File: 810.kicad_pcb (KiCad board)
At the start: 2 copper layers, 148 x 110 mm, 308 parts, among them J1 PJ301BM, J10 PJ301BM, J11 PJ301BM, J12 PJ301BM, J13 PJ301BM, J14 PJ301BM, J15 JACK_MONO_SW, J16 PJ301BM, J17 PJ301B, J18 PJ301B, J2 PJ301BM, J3 PJ301BM, J4 PJ301B, J5 PJ301B, J6 PJ301BM, J7 PJ301BM, J8 PJ301BM, J9 PJ301BM, P1 CONN_01X08, P2 CONN_02X05, P3 CONN_01X03, P4 CONN_01X08, Q1 PMBT2369, Q10 2SK208-GR, Q11 2SC4738, Q12 2SA1832, Q13 2SA1832, Q14 2SA1832, Q15 2SC4738, Q2 2SK208-GR, Q3 2SA1618, Q4 2SC4207, Q5 2SK208-GR, Q6 MMBF4391LT1G, Q7 2SA1832, Q8 PMBT2369, Q9 2SK208-GR, SW1 SPDT, SW2 SPDT, SW3 BF3-1050, SW4 SPDT, SW5 DP6T-ALPHA-SR2511, U1 TL072-, U10 TL072-, U11 TL072-, U12 TA75S558F, U13 TA75S558F, U14 TA75S558F, U15 TA75S558F, U16 TA75S558F, U17 CD4052, U18 TA75S558F, U2 TL072-, U3 TL072-, U4 CD40106, U5 CD4027, U6 LM13700, U7 LM13700, U8 LM13700, U9 TL072-

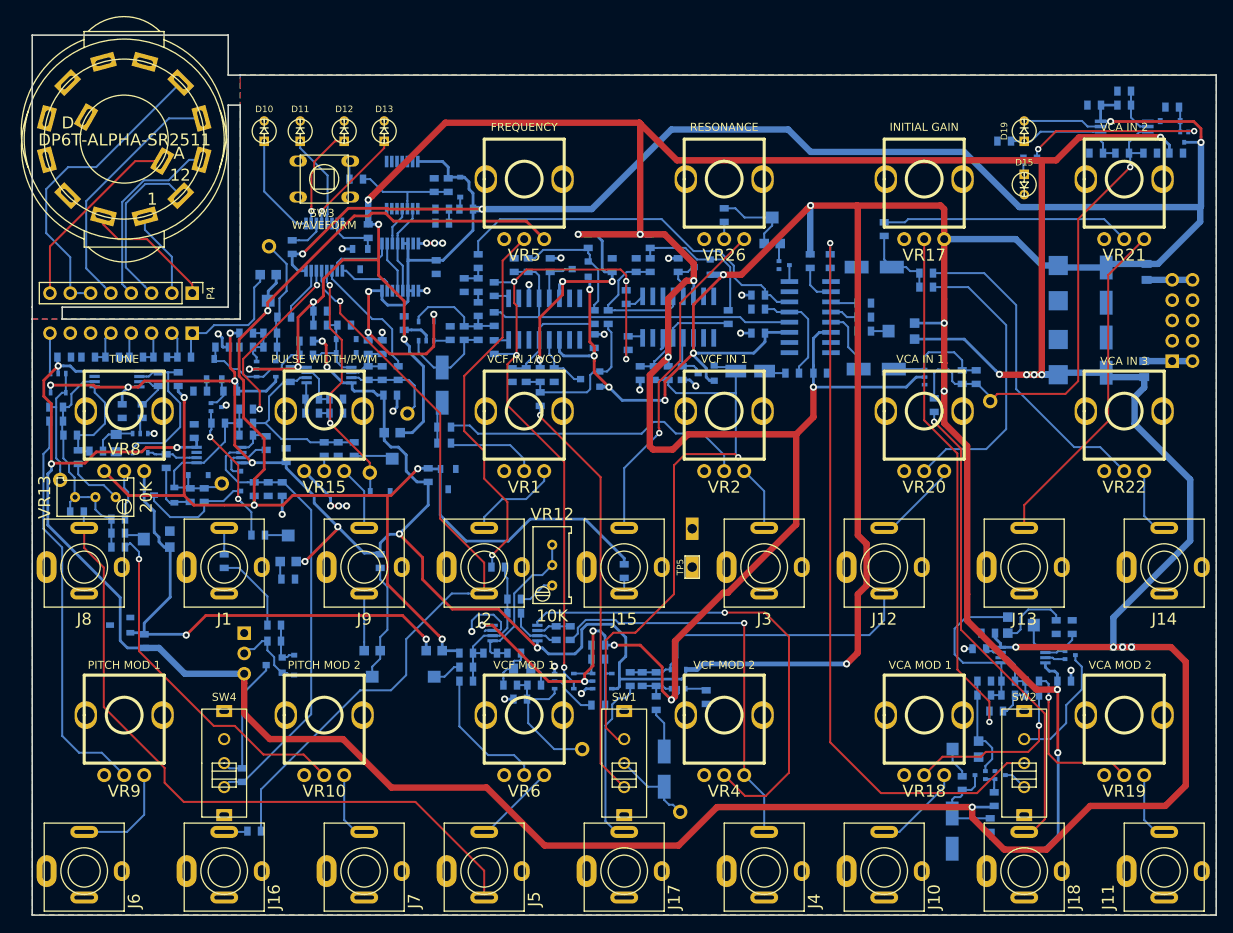
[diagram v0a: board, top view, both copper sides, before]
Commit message: more routing and tweaking. Still need to change 2SK208 footprints
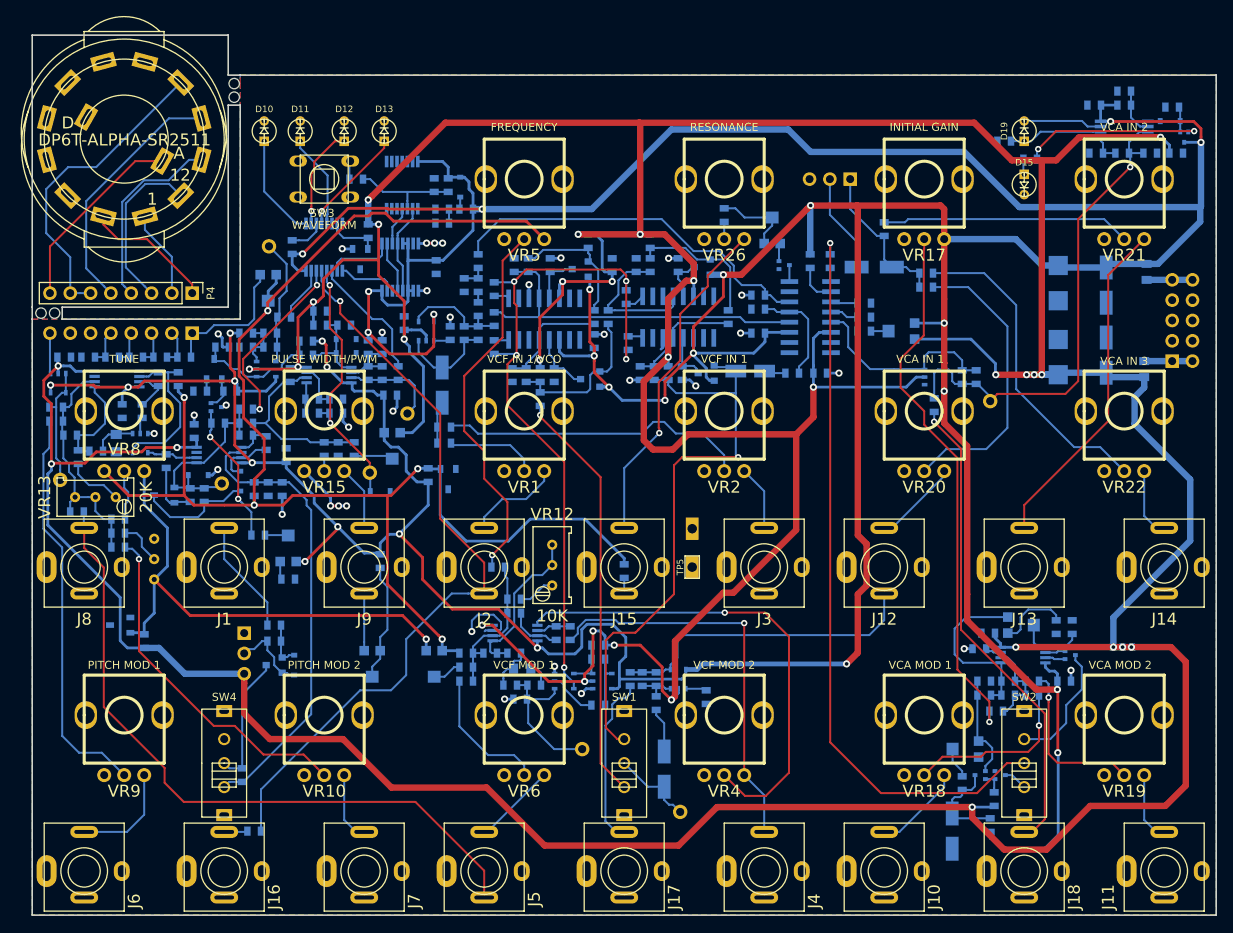
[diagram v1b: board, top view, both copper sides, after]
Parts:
- removed C20: 10μF, MyModules:jrl_c_elec_5x5.3
- removed R5: 100K, MyModules:SM0603-R-JRL
- added P5: CONN_01X02, Pin_Headers:Pin_Header_Straight_1x03_Pitch2.54mm, B.Cu at (186.2, 59.0)
- added TP7: TEST_POINT, MyModules:TEST_POINT_5000_SERIES, B.Cu at (109.2, 47.1)
- added TP7: TEST_POINT, MyModules:TEST_POINT_5000_SERIES, B.Cu at (109.2, 48.8)
- added TP7: TEST_POINT, MyModules:TEST_POINT_5000_SERIES, B.Cu at (85.1, 75.8)
- added TP7: TEST_POINT, MyModules:TEST_POINT_5000_SERIES, B.Cu at (86.8, 75.8)
- VR11: footprint MyModules:TC33X-2 -> MyModules:Bourns-3296W
- moved VR11 2.50 mm to (99.2, 106.5), turned to 0 degrees
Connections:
- C22 pad 1: Net-(C20-Pad1) -> Net-(C22-Pad1)
- J1 pad 3: Net-(J1-Pad3) -> Net-(C1-Pad1)
- R110 pad 1: Net-(C20-Pad1) -> Net-(C22-Pad1)
- U16 pad 3: Net-(C20-Pad1) -> Net-(C22-Pad1)
- U8 pad 5: Net-(C20-Pad2) -> Net-(C22-Pad1)
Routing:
- net Net-(C22-Pad1): track 0.00 -> 25.6 mm
- net Net-(C20-Pad1): track 13.8 -> 0.00 mm
- net Net-(C15-Pad1): track 7.91 -> 20.3 mm
- net Net-(C15-Pad2): track 9.95 -> 19.3 mm
- net Net-(C20-Pad2): track 8.19 -> 0.00 mm
- net GND: track 50.4 -> 57.8 mm, vias 28 -> 33
- net Net-(C1-Pad1): track 10.5 -> 14.4 mm
- net Net-(R32-Pad1): track 2.66 -> 5.96 mm
- net Net-(J1-Pad3): track 3.30 -> 0.00 mm
- net Net-(R73-Pad1): track 65.1 -> 67.5 mm
- net -12V: track 774.6 -> 776.4 mm
- net -10V: track 64.4 -> 63.3 mm, vias 2 -> 1
- net Net-(R31-Pad1): track 44.3 -> 43.7 mm

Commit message: added secret sub-oscillator
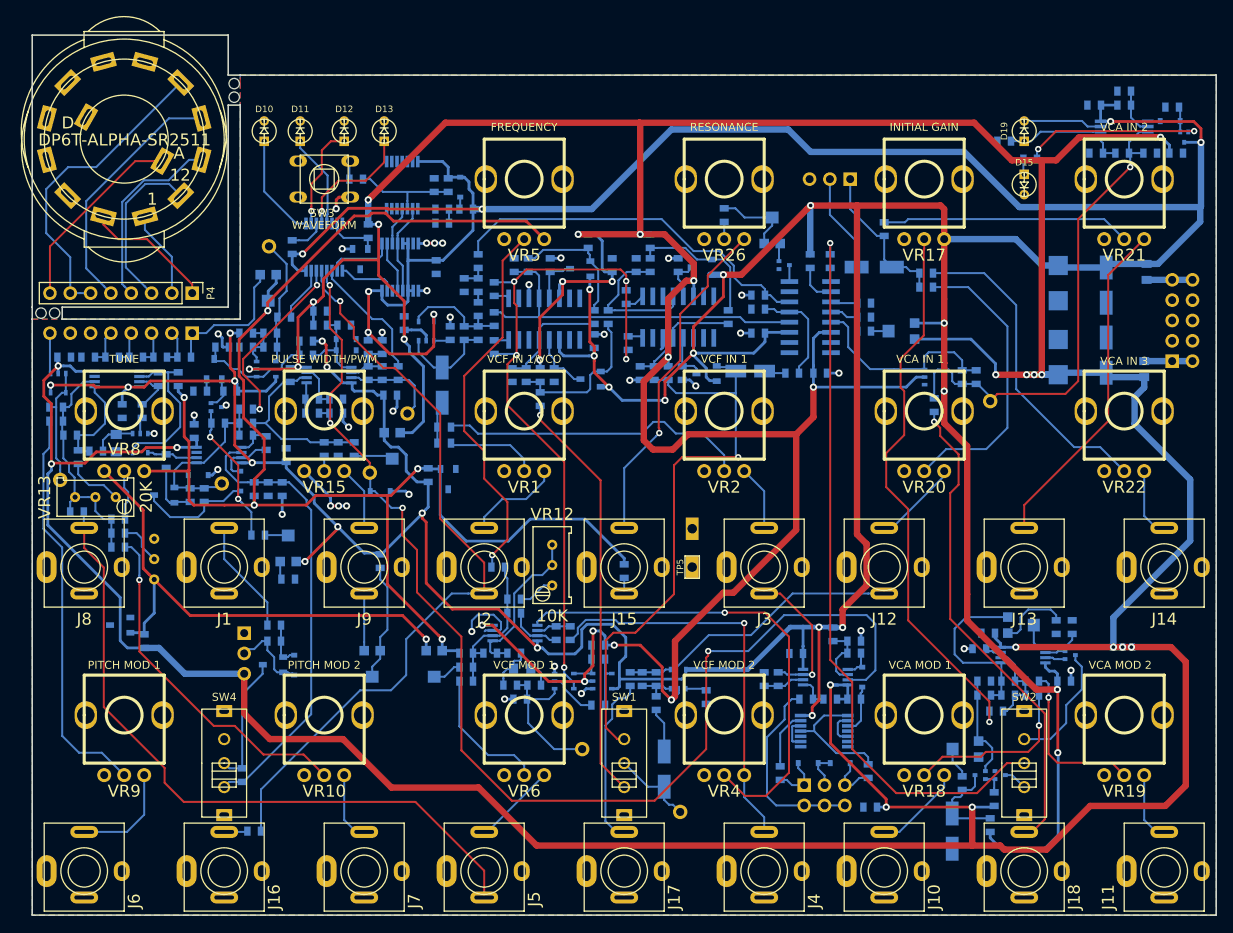
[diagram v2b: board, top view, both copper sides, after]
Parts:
- added C20: 47p, MyModules:SM0603-C-JRL, B.Cu at (186.8, 118.2)
- added C47: 0.1µ, MyModules:SM0603-C-JRL, B.Cu at (179.5, 118.3)
- added C48: 0.1µ, MyModules:SM0603-C-JRL, B.Cu at (188.8, 137.5)
- added D20: 1N4148, MyModules:SOD323-C1A2, B.Cu at (187.8, 121.2)
- added D21: 1N4148, MyModules:SOD323-C1A2, B.Cu at (181.0, 132.0)
- added D22: 1N4148, MyModules:SOD323-C1A2, B.Cu at (185.0, 132.0)
- added P6: CONN_02X03, Pin_Headers:Pin_Header_Straight_2x03_Pitch2.54mm, B.Cu at (180.5, 134.8)
- added R143: 220K, MyModules:SM0603-R-JRL, B.Cu at (184.1, 115.9)
- added R144: 68K, MyModules:SM0603-R-JRL, B.Cu at (186.8, 124.0)
- added R145: 47K, MyModules:SM0603-R-JRL, B.Cu at (177.5, 133.2)
- added R146: 47K, MyModules:SM0603-R-JRL, B.Cu at (188.5, 133.0)
- added R147: 47K, MyModules:SM0603-R-JRL, B.Cu at (180.8, 124.0)
- added R148: 100K, MyModules:SM0603-R-JRL, B.Cu at (175.5, 121.5)
- added R149: 120K, MyModules:SM0603-R-JRL, B.Cu at (183.8, 124.0)
- added R150: 33K, MyModules:SM0603-R-JRL, B.Cu at (177.2, 121.5)
- added R5: 10K, MyModules:SM0603-R-JRL, B.Cu at (186.8, 116.8)
- added U19: TL072-, MyModules:TSSOP8-JRL, B.Cu at (183.2, 121.2)
- added U20: CD4013, Housings_SSOP:TSSOP-14_4.4x5mm_Pitch0.65mm, B.Cu at (183.0, 128.0)
- Q1, Q10, Q2, Q9: footprint TO_SOT_Packages_SMD:SOT-23 -> MyModules:SOT23-132-JRL
- Q5: footprint TO_SOT_Packages_SMD:SC-59 -> MyModules:SOT23-132-JRL
- moved D8 0.35 mm to (123.2, 80.4)
- moved Q1 0.16 mm to (114.1, 119.7), turned to 270 degrees
- moved Q10 0.07 mm to (168.3, 83.3), turned to 270 degrees
- moved Q5 0.05 mm to (153.8, 84.0), turned to 270 degrees
- moved Q9 0.05 mm to (167.7, 70.0), turned to 270 degrees
- turned Q2 to 270 degrees
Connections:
- J3 pad 2: Net-(J3-Pad2) -> SUB_OSC
- VR8 pad 1: +10V -> -10V
- VR8 pad 3: -10V -> +10V
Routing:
- net VCO_PULSE: track 33.6 -> 153.1 mm, vias 2 -> 4
- net -12V: track 776.4 -> 812.9 mm, vias 32 -> 34
- net Net-(P6-Pad2): track 0.00 -> 25.3 mm
- net SUB_OSC: track 0.00 -> 18.2 mm, vias 0 -> 1
- net Net-(R146-Pad1): track 0.00 -> 16.1 mm
- net +12V: track 732.2 -> 748.2 mm, vias 30 -> 32
- net Net-(C20-Pad1): track 0.00 -> 8.14 mm
- net Net-(R145-Pad1): track 0.00 -> 7.33 mm
- net GND: track 57.8 -> 64.6 mm, vias 33 -> 36
- net Net-(D21-Pad2): track 0.00 -> 6.54 mm
- net Net-(D22-Pad2): track 0.00 -> 6.53 mm
- net Net-(D20-Pad1): track 0.00 -> 6.21 mm
- net +10V: track 193.6 -> 188.0 mm
- net Net-(R148-Pad2): track 0.00 -> 5.18 mm
- net Net-(D21-Pad1): track 0.00 -> 4.59 mm
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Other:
- board text removed: "810"

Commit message: board tweaking, getting ready to match up with panel art and order second prototype
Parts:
- VR11, VR12, VR13: footprint MyModules:Bourns-3296W -> MyModules:TT-BI-67W
- moved R126 0.75 mm to (208.8, 55.8)
- moved D11 0.71 mm to (118.0, 52.5)
- moved D15 0.67 mm to (208.0, 59.0)
- moved VR13 0.50 mm to (92.4, 98.7)
- moved D10 0.50 mm to (113.0, 52.5)
- moved D12 0.50 mm to (123.0, 52.5)
- moved D13 0.50 mm to (128.0, 52.5)
- moved D19 0.50 mm to (208.0, 52.5)
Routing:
- net Net-(D11-Pad2): track 11.7 -> 12.8 mm
- net Net-(Q15-Pad2): track 22.5 -> 21.6 mm
- net Net-(D12-Pad2): track 13.0 -> 13.8 mm
- net Net-(D13-Pad2): track 15.5 -> 16.0 mm
- net Net-(D10-Pad2): track 13.2 -> 13.7 mm
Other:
- board text added: "TRI SYM"
- board text added: "r1.1 01/18"
- board text removed: "r1.0 11/17"

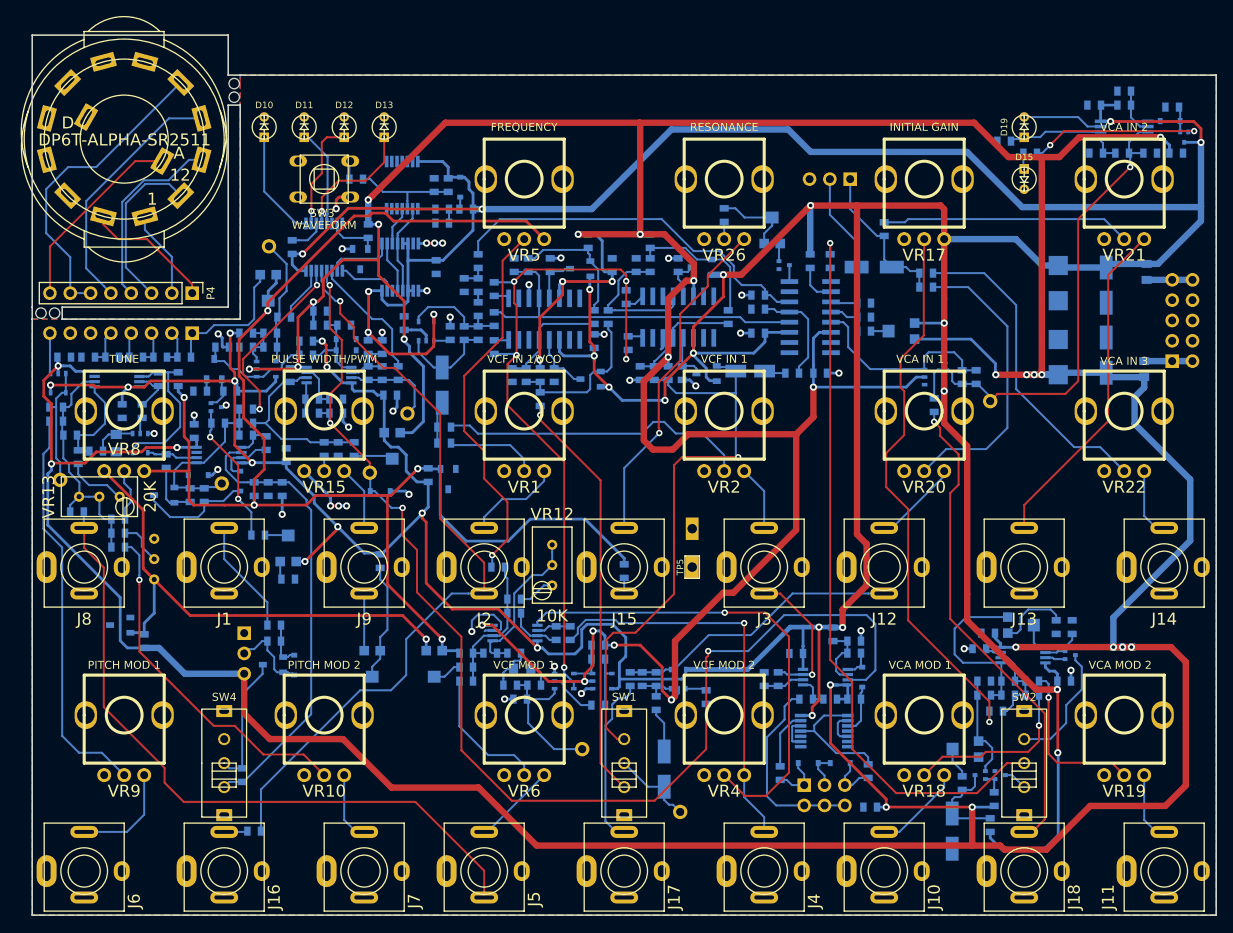
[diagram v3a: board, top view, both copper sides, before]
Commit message: changes switches to horizontal position
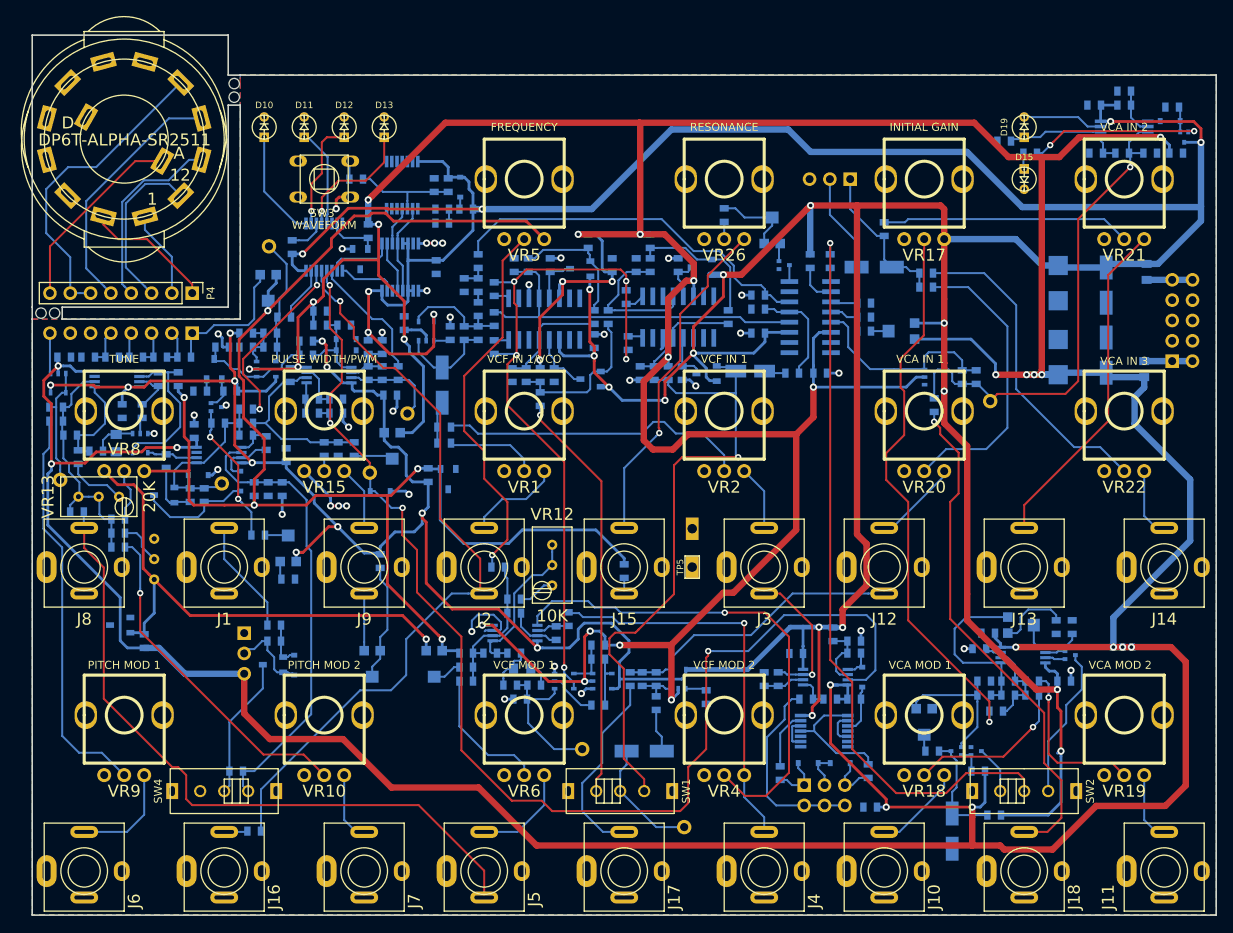
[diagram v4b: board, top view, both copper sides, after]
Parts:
- moved VR24 5.96 mm to (195.5, 127.0), turned to 0 degrees
- moved R99 5.48 mm to (196.5, 130.5), turned to 0 degrees
- moved Q11 4.24 mm to (199.5, 130.5)
- moved Q12 4.24 mm to (202.0, 130.5)
- moved R103 4.03 mm to (202.2, 133.0), turned to 180 degrees
- moved SW1 3.54 mm to (157.5, 135.5), turned to 0 degrees
- moved SW2 3.50 mm to (208.0, 135.5), turned to 0 degrees
- moved SW4 3.50 mm to (108.0, 135.5), turned to 180 degrees
- moved C23 3.36 mm to (160.5, 130.5), turned to 0 degrees
- moved TP4 1.96 mm to (165.5, 140.0)
- moved R13 1.77 mm to (151.0, 114.0), turned to 90 degrees
- moved R107 1.35 mm to (204.2, 138.5), turned to 0 degrees
- moved R135 0.90 mm to (109.5, 133.0), turned to 0 degrees
- moved VR13 0.08 mm to (92.3, 98.7)
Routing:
- net Net-(C21-Pad2): track 74.9 -> 81.4 mm
- net Net-(Q11-Pad1): track 12.9 -> 17.9 mm
- net Net-(C23-Pad2): track 10.5 -> 15.2 mm
- net +12V: track 748.4 -> 744.4 mm
- net VCO_PULSE: track 153.1 -> 156.8 mm
- net Net-(Q13-Pad3): track 15.7 -> 19.1 mm
- net Net-(J18-Pad3): track 60.8 -> 64.0 mm
- net Net-(C26-Pad1): track 12.1 -> 15.1 mm
- net Net-(Q12-Pad3): track 2.97 -> 6.00 mm
- net Net-(J17-Pad3): track 21.6 -> 24.5 mm
- net Net-(J5-Pad3): track 10.4 -> 12.6 mm
- net Net-(R99-Pad1): track 3.90 -> 2.11 mm
- net Net-(U9-Pad5): track 61.1 -> 62.7 mm
- net Net-(R31-Pad1): track 43.8 -> 42.3 mm
- net -12V: track 812.9 -> 811.4 mm
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
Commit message: ordered PCB v1-1
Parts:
- added G***: LOGO, LOGO, B.Cu at (132.2, 131.8)
- added G***: LOGO, LOGO, B.Cu at (157.8, 96.5)
- moved VR14 12.8 mm to (125.5, 107.0), turned to 180 degrees
- moved R55 2.14 mm to (128.2, 104.8)
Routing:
- net Net-(R55-Pad1): track 14.9 -> 6.44 mm
- net Net-(J9-Pad2): track 8.15 -> 3.41 mm
- net -12V: track 811.4 -> 814.9 mm
- net VCO: track 95.8 -> 93.8 mm
- net +12V: track 744.4 -> 742.9 mm
- net +10V: track 187.5 -> 188.1 mm
